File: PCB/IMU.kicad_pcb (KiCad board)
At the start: 2 copper layers, 68 parts, among them IC1 STM32F405VGT, IC2 ADP3335ARMZ-3.3, IC3 ADP3335ARMZ-5, IC4 MS5611-01BA03, P1 UART1, P2 SWD, P3 UART2, P4 SPI, P5 BATTERY, P6 USB_OTG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

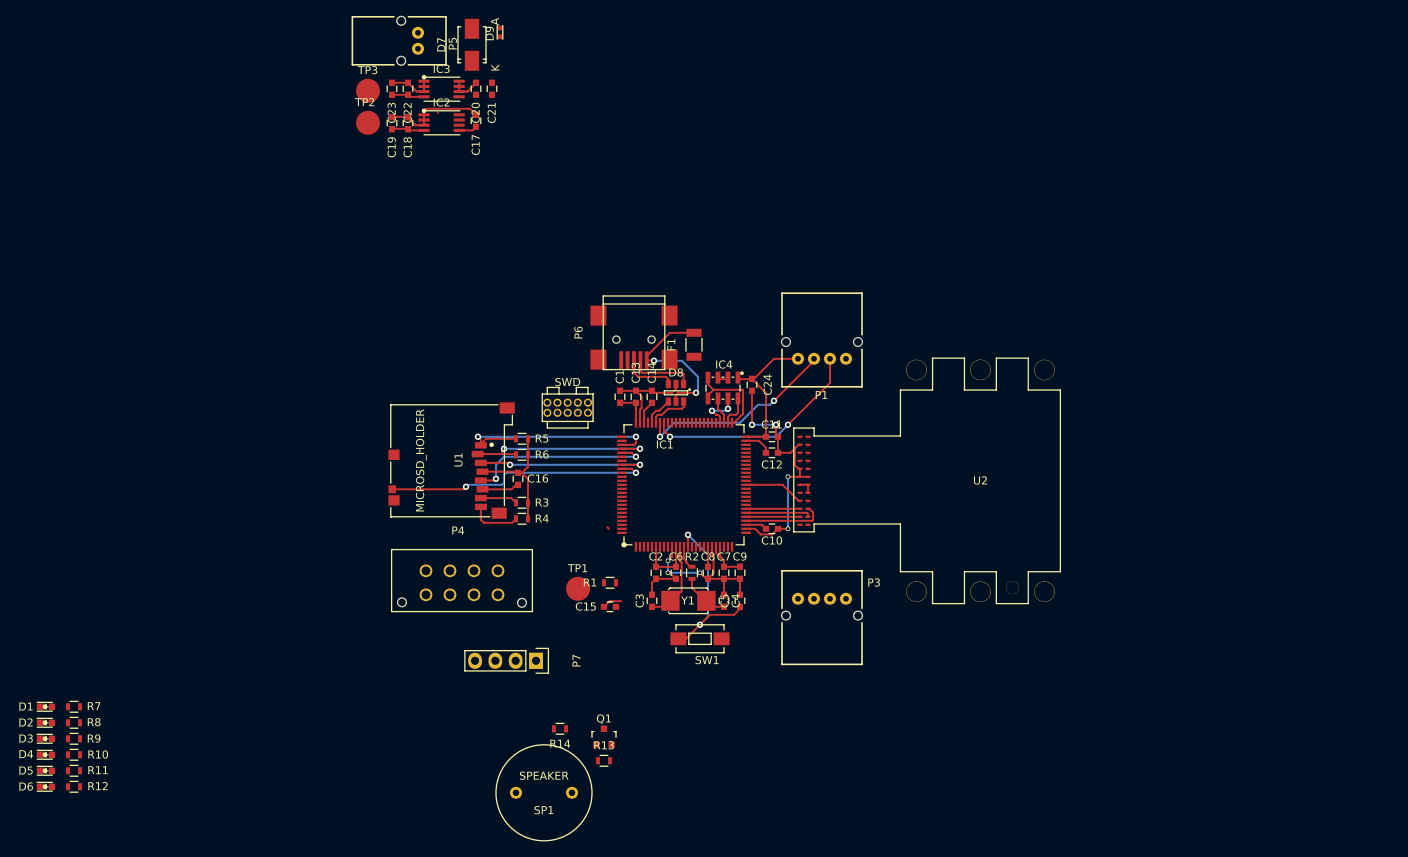
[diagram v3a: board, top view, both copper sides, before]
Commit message: Move components to likely final locations and adjust some trace widths
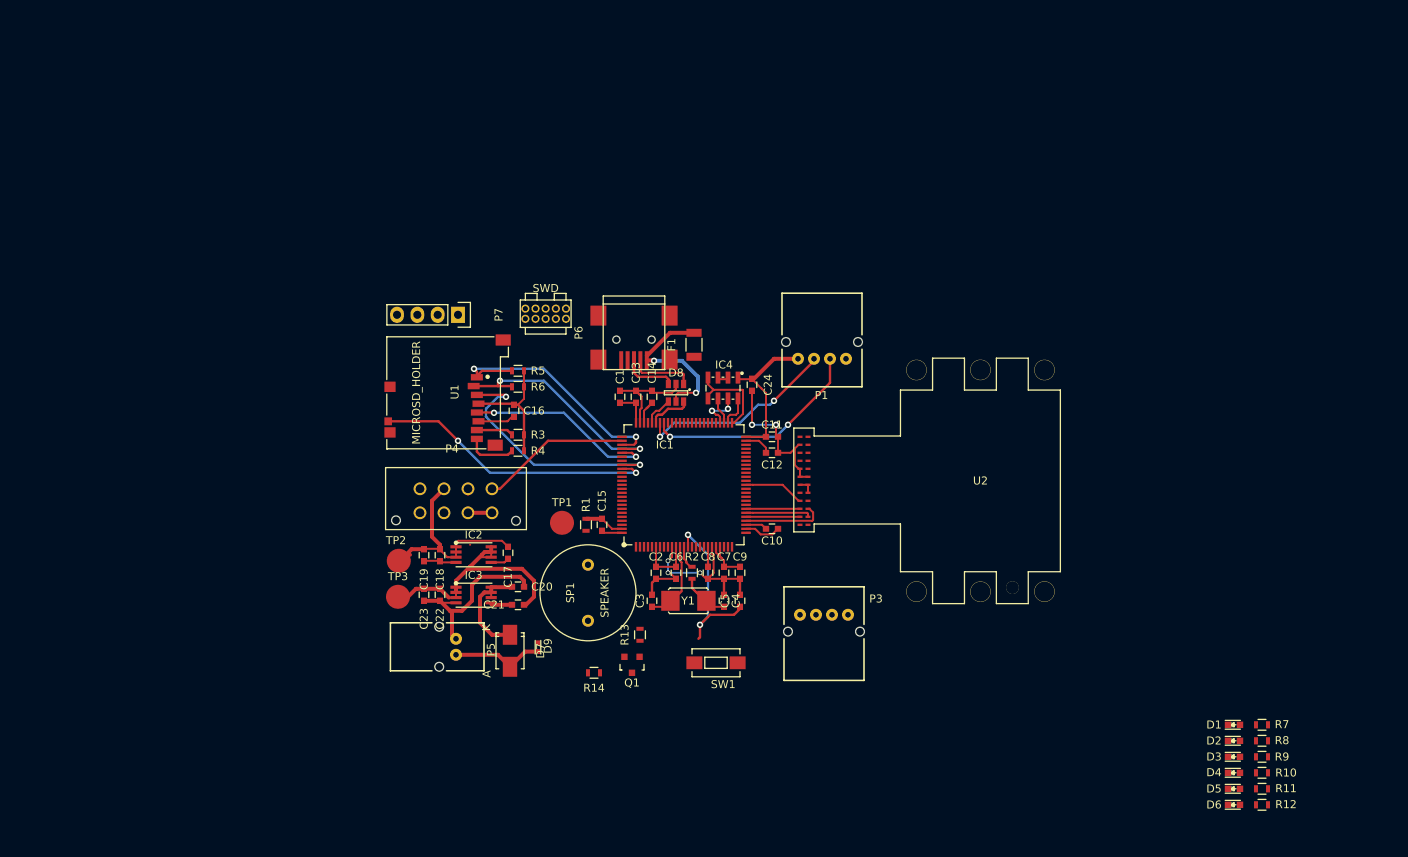
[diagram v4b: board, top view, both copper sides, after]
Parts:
- moved D1 148.5 mm to (250.2, 133.0)
- moved D2 148.5 mm to (250.2, 135.0)
- moved D3 148.5 mm to (250.2, 137.0)
- moved D4 148.5 mm to (250.2, 139.0)
- moved D5 148.5 mm to (250.2, 141.0)
- moved D6 148.5 mm to (250.2, 143.0)
- moved R10 148.5 mm to (253.8, 139.0)
- moved R11 148.5 mm to (253.8, 141.0)
- moved R12 148.5 mm to (253.8, 143.0)
- moved R7 148.5 mm to (253.8, 133.0)
- moved R8 148.5 mm to (253.8, 135.0)
- moved R9 148.5 mm to (253.8, 137.0)
- moved D7 75.9 mm to (159.8, 123.8), turned to 270 degrees
- moved D9 75.9 mm to (163.2, 122.8), turned to 270 degrees
- moved P5 75.9 mm to (153.0, 124.2)
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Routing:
- net +5V: track 7.76 -> 34.2 mm
- net SPI3_NSS: track 0.00 -> 18.7 mm
- net +3V3: track 72.4 -> 88.1 mm
- net GND: track 88.9 -> 103.9 mm, vias 7 -> 5
- net Net-(D7-Pad2): track 0.00 -> 11.7 mm
- net SDIO_CMD: track 22.2 -> 31.8 mm
- net +BATT: track 3.87 -> 13.2 mm
- net SDIO_D3: track 24.8 -> 28.9 mm
- net SDIO_D2: track 28.4 -> 32.4 mm
- net Net-(C21-Pad2): track 0.62 -> 3.42 mm
- net /SDCard/CARD_DETECT: track 33.9 -> 35.6 mm
- net ~RST: track 23.7 -> 22.1 mm
- net SPI3_MISO: track 0.00 -> 0.75 mm
- net SDIO_CK: track 23.6 -> 24.1 mm
- net /DATA_RDY: track 0.00 -> 0.50 mm
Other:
- net class Power: trace_width 0.3 -> 0.5

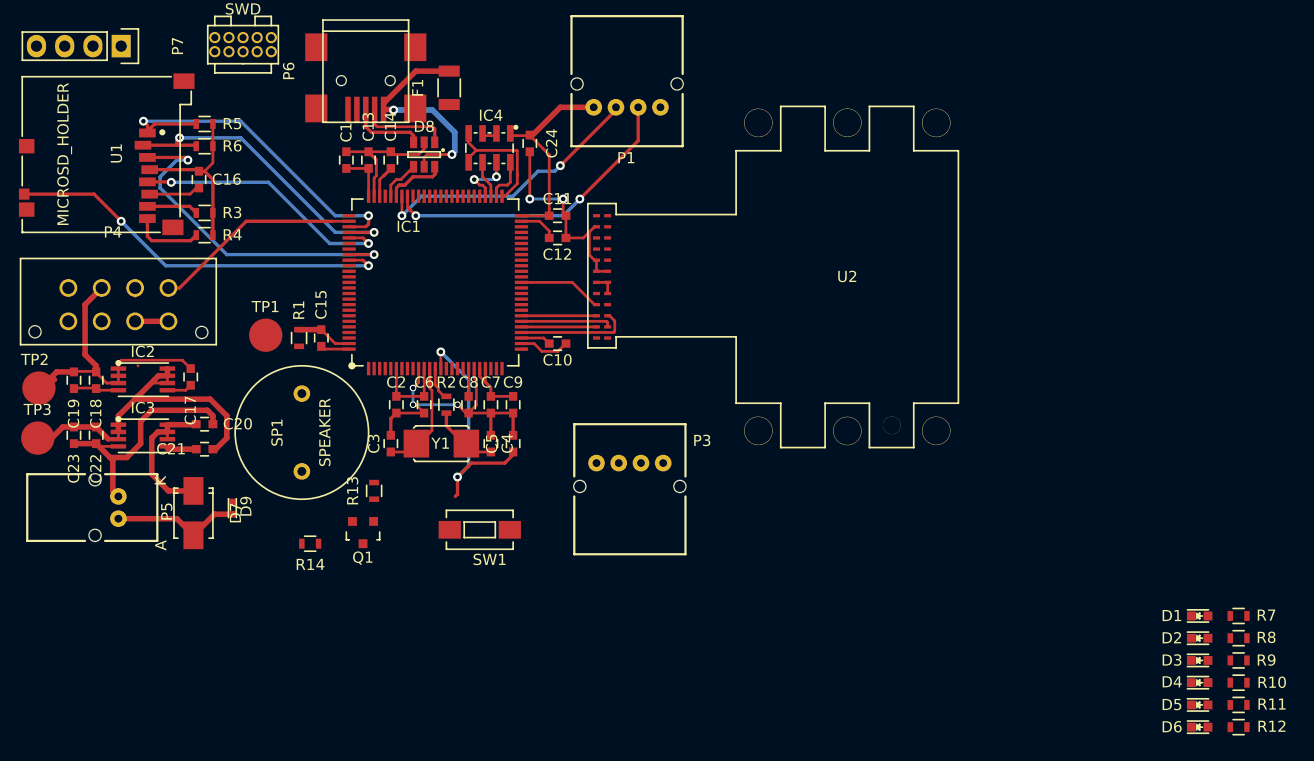
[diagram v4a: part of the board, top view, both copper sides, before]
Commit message: Begin routing SPI3 and place LEDs on board
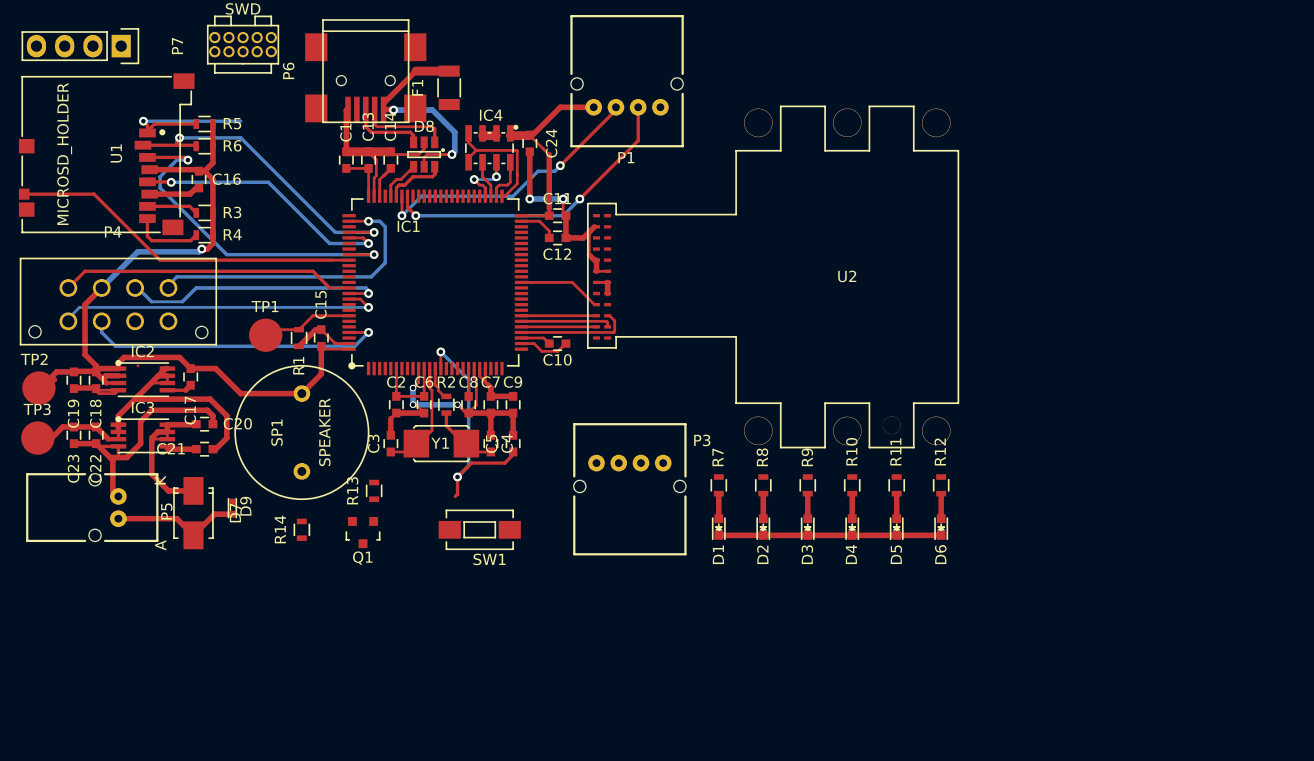
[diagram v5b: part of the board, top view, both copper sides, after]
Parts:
- moved R7 48.2 mm to (207.0, 121.2), turned to 90 degrees
- moved R8 44.9 mm to (211.0, 121.2), turned to 90 degrees
- moved D1 44.0 mm to (207.0, 125.0), turned to 90 degrees
- moved R9 41.8 mm to (215.0, 121.2), turned to 90 degrees
- moved D2 40.5 mm to (211.0, 125.0), turned to 90 degrees
- moved R10 39.0 mm to (219.0, 121.2), turned to 90 degrees
- moved D3 37.2 mm to (215.0, 125.0), turned to 90 degrees
- moved R11 36.5 mm to (223.0, 121.2), turned to 90 degrees
- moved R12 34.5 mm to (227.0, 121.2), turned to 90 degrees
- moved D4 34.2 mm to (219.0, 125.0), turned to 90 degrees
- moved D5 31.6 mm to (223.0, 125.0), turned to 90 degrees
- moved D6 29.4 mm to (227.0, 125.0), turned to 90 degrees
- moved R14 1.46 mm to (169.5, 125.2), turned to 90 degrees
- turned R1 to 90 degrees
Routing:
- net +3V3: track 88.1 -> 118.8 mm, vias 0 -> 1
- net SPI3_MOSI: track 0.00 -> 29.7 mm, vias 0 -> 1
- net /DATA_RDY: track 0.50 -> 27.8 mm, vias 0 -> 1
- net SPI3_SCK: track 0.00 -> 26.5 mm
- net GND: track 103.9 -> 128.9 mm
- net SPI3_MISO: track 0.75 -> 24.1 mm, vias 0 -> 1
- net SDIO_D2: track 32.4 -> 14.8 mm, vias 2 -> 1
- net /BOOT0: track 0.00 -> 8.97 mm
- net SPI3_NSS: track 18.7 -> 27.3 mm, vias 0 -> 1
- net /SDCard/CARD_DETECT: track 35.6 -> 31.7 mm, vias 2 -> 0
- net Net-(D6-Pad2): track 0.00 -> 2.25 mm
- net Net-(D5-Pad2): track 0.00 -> 2.25 mm
- net Net-(D4-Pad2): track 0.00 -> 2.25 mm
- net Net-(D3-Pad2): track 0.00 -> 2.25 mm
- net Net-(D2-Pad2): track 0.00 -> 2.25 mm
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
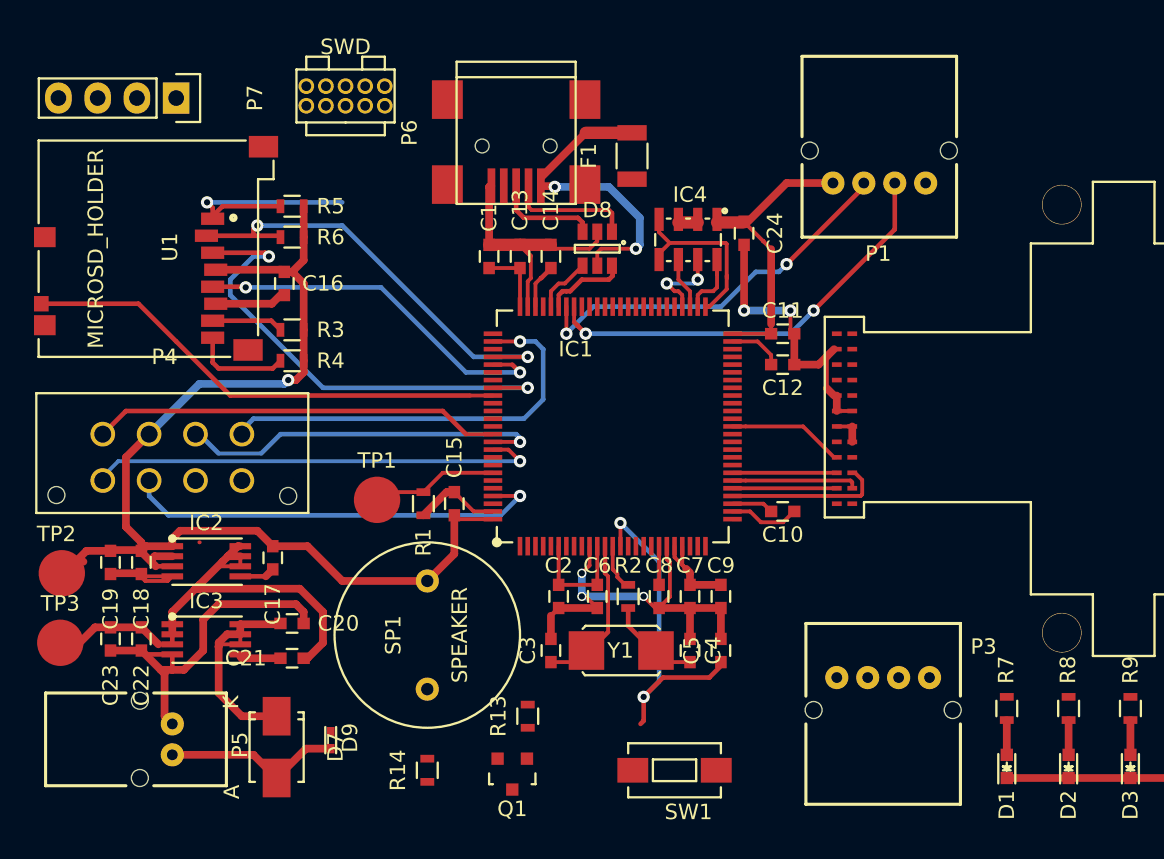
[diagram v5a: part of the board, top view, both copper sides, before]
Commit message: Move status LED outputs to pins 33 to 36 of the microcontroller
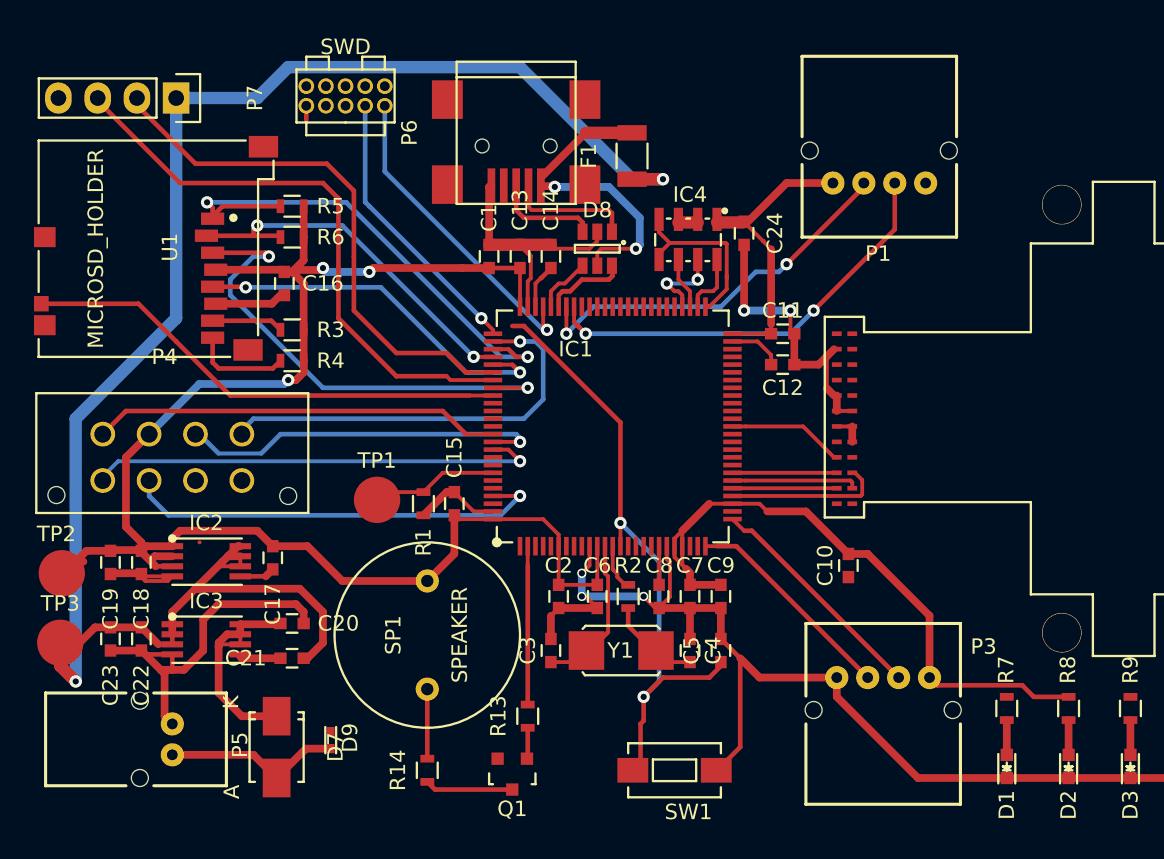
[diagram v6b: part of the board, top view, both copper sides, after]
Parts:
- moved C10 5.51 mm to (196.8, 112.0), turned to 270 degrees
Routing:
- net +5V: track 34.6 -> 115.3 mm, vias 0 -> 2
- net +3V3: track 118.8 -> 169.9 mm, vias 1 -> 3
- net /CAN1_TX: track 0.00 -> 37.8 mm
- net /CAN1_RX: track 0.00 -> 35.2 mm
- net GND: track 128.9 -> 155.2 mm
- net /SWDIO: track 0.00 -> 20.6 mm, vias 0 -> 1
- net ~RST: track 22.1 -> 42.3 mm
- net SDIO_D2: track 14.8 -> 33.4 mm, vias 1 -> 2
- net /SWDCLK: track 0.00 -> 18.2 mm, vias 0 -> 1
- net USART2_RX: track 0.45 -> 15.4 mm
- net USART2_TX: track 0.00 -> 14.0 mm
- net /StatusIndicators/Buzzer: track 0.00 -> 10.2 mm
- net Net-(Q1-Pad3): track 0.00 -> 5.71 mm
- net SDIO_D3: track 28.9 -> 24.4 mm
- net Net-(R14-Pad2): track 0.00 -> 4.50 mm
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
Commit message: Finish routing PCB
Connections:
- IC1 pad 1: /StatusIndicators/~IMU -> Net-(IC1-Pad1)
- IC1 pad 3: /StatusIndicators/Sensors -> Net-(IC1-Pad3)
- IC1 pad 33: Net-(IC1-Pad33) -> /StatusIndicators/Sensors
- IC1 pad 34: Net-(IC1-Pad34) -> /StatusIndicators/~Sensors
- IC1 pad 35: Net-(IC1-Pad35) -> /StatusIndicators/IMU
- IC1 pad 36: Net-(IC1-Pad36) -> /StatusIndicators/~IMU
- IC1 pad 4: /StatusIndicators/~Sensors -> Net-(IC1-Pad4)
- IC1 pad 98: /StatusIndicators/IMU -> Net-(IC1-Pad98)
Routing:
- net SDIO_D1: track 6.36 -> 58.2 mm, vias 0 -> 2
- net +5V: track 115.3 -> 165.8 mm, vias 2 -> 6
- net /StatusIndicators/~IMU: track 0.00 -> 47.8 mm, vias 0 -> 2
- net SDIO_D0: track 4.63 -> 50.1 mm, vias 0 -> 2
- net /StatusIndicators/IMU: track 0.00 -> 43.2 mm, vias 0 -> 2
- net +3V3: track 169.9 -> 210.1 mm
- net /StatusIndicators/~Sensors: track 0.00 -> 39.2 mm, vias 0 -> 2
- net ~RST: track 42.3 -> 81.3 mm, vias 2 -> 3
- net /StatusIndicators/Sensors: track 0.00 -> 33.9 mm, vias 0 -> 2
- net GND: track 155.2 -> 180.9 mm, vias 5 -> 16
- net /SWDIO: track 20.6 -> 24.6 mm
- net USART1_RX: track 25.5 -> 26.8 mm
- net USART1_TX: track 27.9 -> 28.8 mm
- net +BATT: track 14.8 -> 14.1 mm
- net /CAN1_RX: track 35.2 -> 35.5 mm, vias 0 -> 1
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- added copper zone on B.Cu, net GND
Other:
- board outline added: 86.2 x 49.8 mm

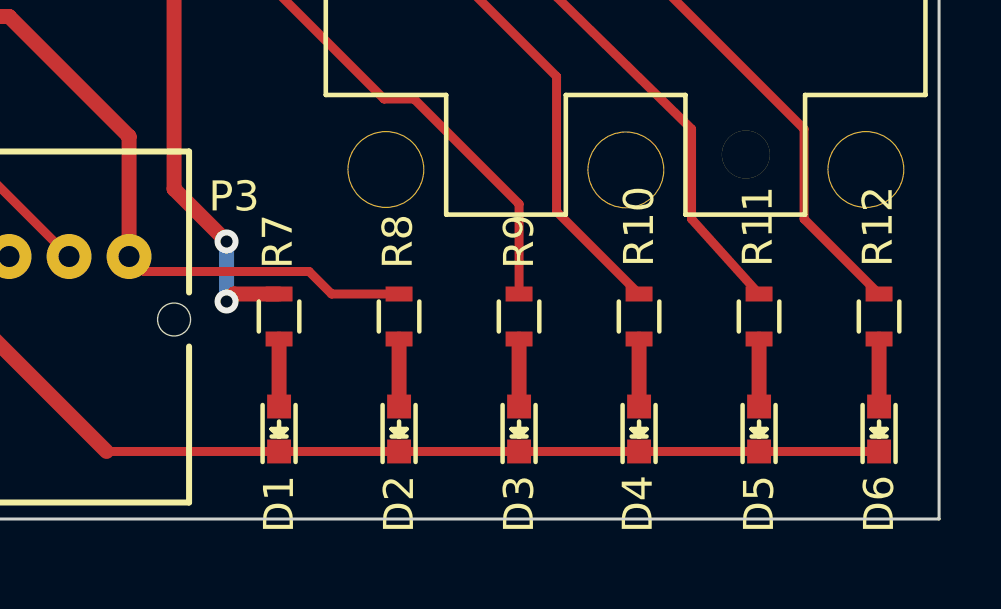
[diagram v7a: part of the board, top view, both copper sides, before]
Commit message: Add silkscreen labels to LEDs
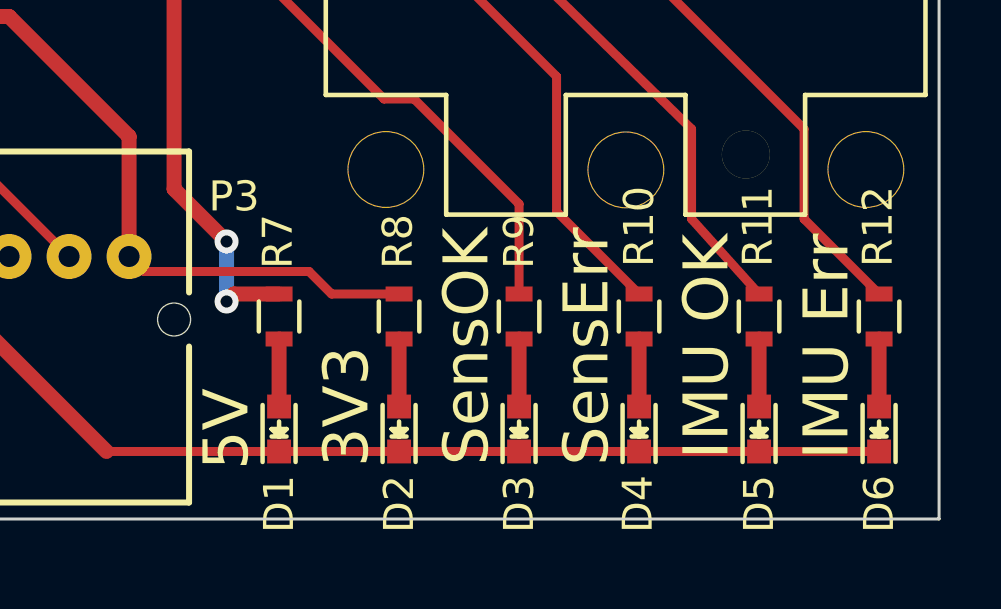
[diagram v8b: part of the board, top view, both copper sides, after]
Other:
- board text added: "3V3"
- board text added: "5V"
- board text added: "IMU Err"
- board text added: "IMU OK"
- board text added: "SensErr"
- board text added: "SensOK"
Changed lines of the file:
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@@
     (links 188)
     (no_connects 3)
-    (area 0 0 0 0)
+    (area 142.699999 78.199999 229.050001 128.050001)
     (thickness 1.6)
-    (drawings 4)
+    (drawings 10)
     (tracks 753)
     (zones 0)
@@
   )
   (setup
-    (last_trace_width 0.3)
+    (last_trace_width 0.25)
     (user_trace_width 0.2)
     (user_trace_width 0.3)
@@
     (pad 32 thru_hole circle (at 22.559899 -19.362802 180) (size 2.5654 2.5654) (drill 2.4892) (layers *.Cu *.Mask F.SilkS))
   )
+  (gr_text "IMU Err" (at 225.25 122.25 90) (layer F.SilkS)
+    (effects (font (size 1.5 1.5) (thickness 0.3)))
+  )
+  (gr_text "IMU OK" (at 221.25 122.25 90) (layer F.SilkS)
+    (effects (font (size 1.5 1.5) (thickness 0.3)))
+  )
+  (gr_text SensErr (at 217.25 122.25 90) (layer F.SilkS)
+    (effects (font (size 1.5 1.5) (thickness 0.3)))
+  )
+  (gr_text SensOK (at 213.25 122.25 90) (layer F.SilkS)
+    (effects (font (size 1.5 1.5) (thickness 0.3)))
+  )
+  (gr_text 3V3 (at 209.25 124.25 90) (layer F.SilkS)
+    (effects (font (size 1.5 1.5) (thickness 0.3)))
+  )
+  (gr_text 5V (at 205.25 125 90) (layer F.SilkS)
+    (effects (font (size 1.5 1.5) (thickness 0.3)))
+  )
   (gr_line (start 142.75 78.25) (end 142.75 128) (angle 90) (layer Edge.Cuts) (width 0.1))
